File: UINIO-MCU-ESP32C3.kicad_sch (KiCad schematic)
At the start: 40 parts, among them J1 Conn_01x15_Male, J2 外接串行下载接口, J3 Conn_01x15_Male, SW1 复位按键, SW2 下载按键, U1 ME6211C33M5G-N, U2 W25Q128JVSSIQ, U3 ESP32-C3, U4 CH343P, Y1 40MHz

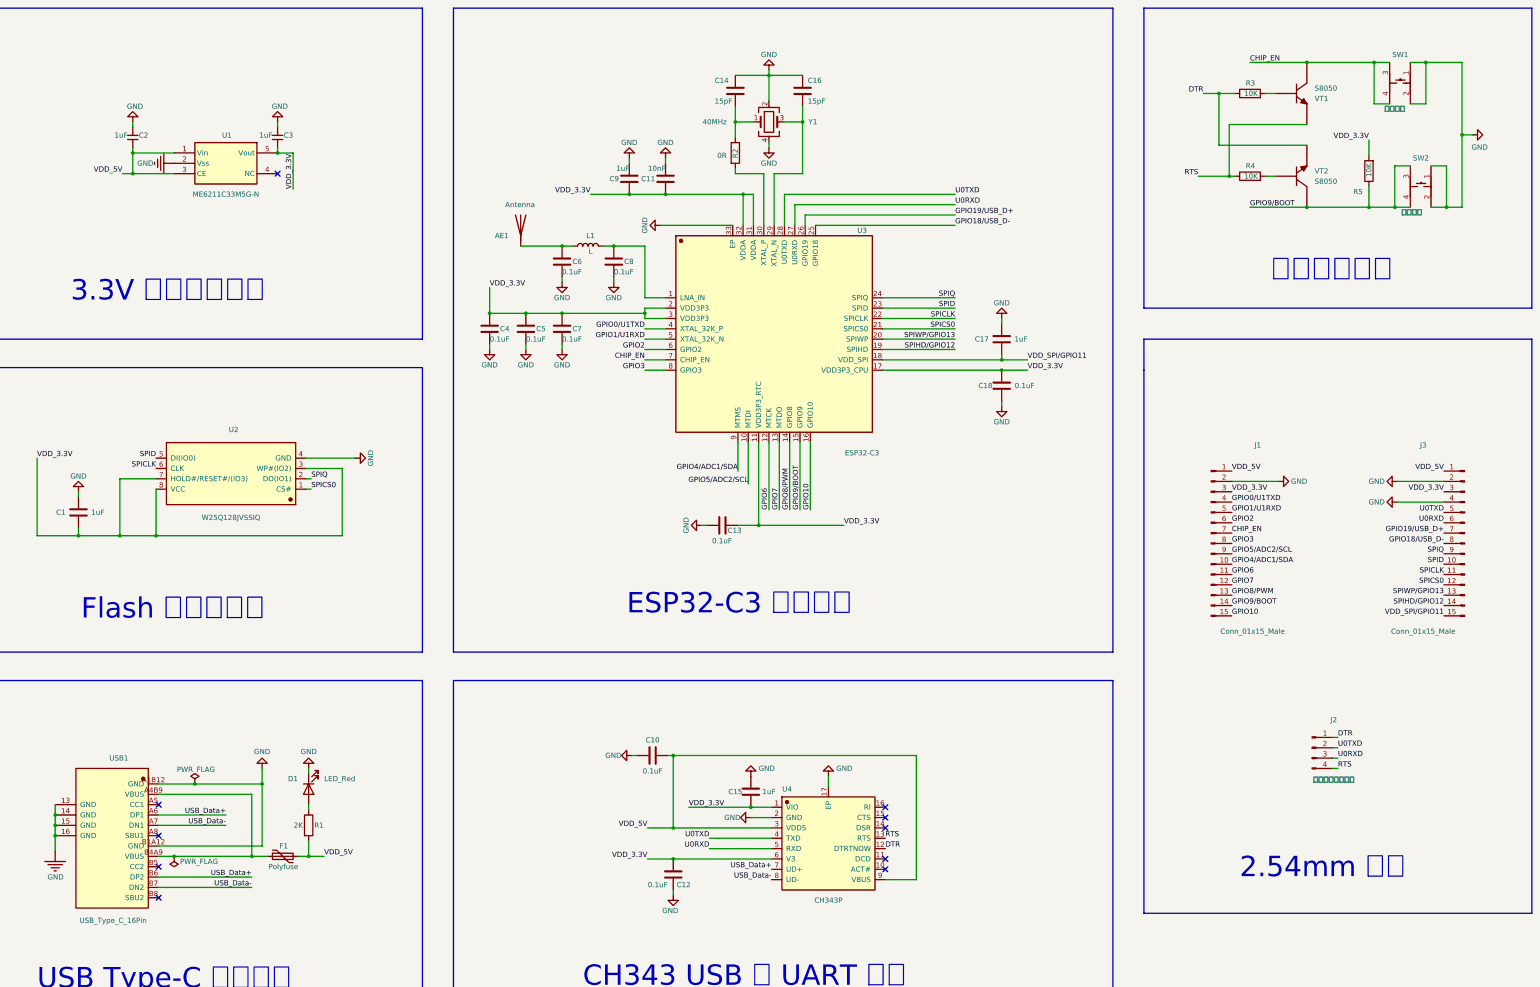
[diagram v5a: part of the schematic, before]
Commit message: The schematic diagram is drawn.
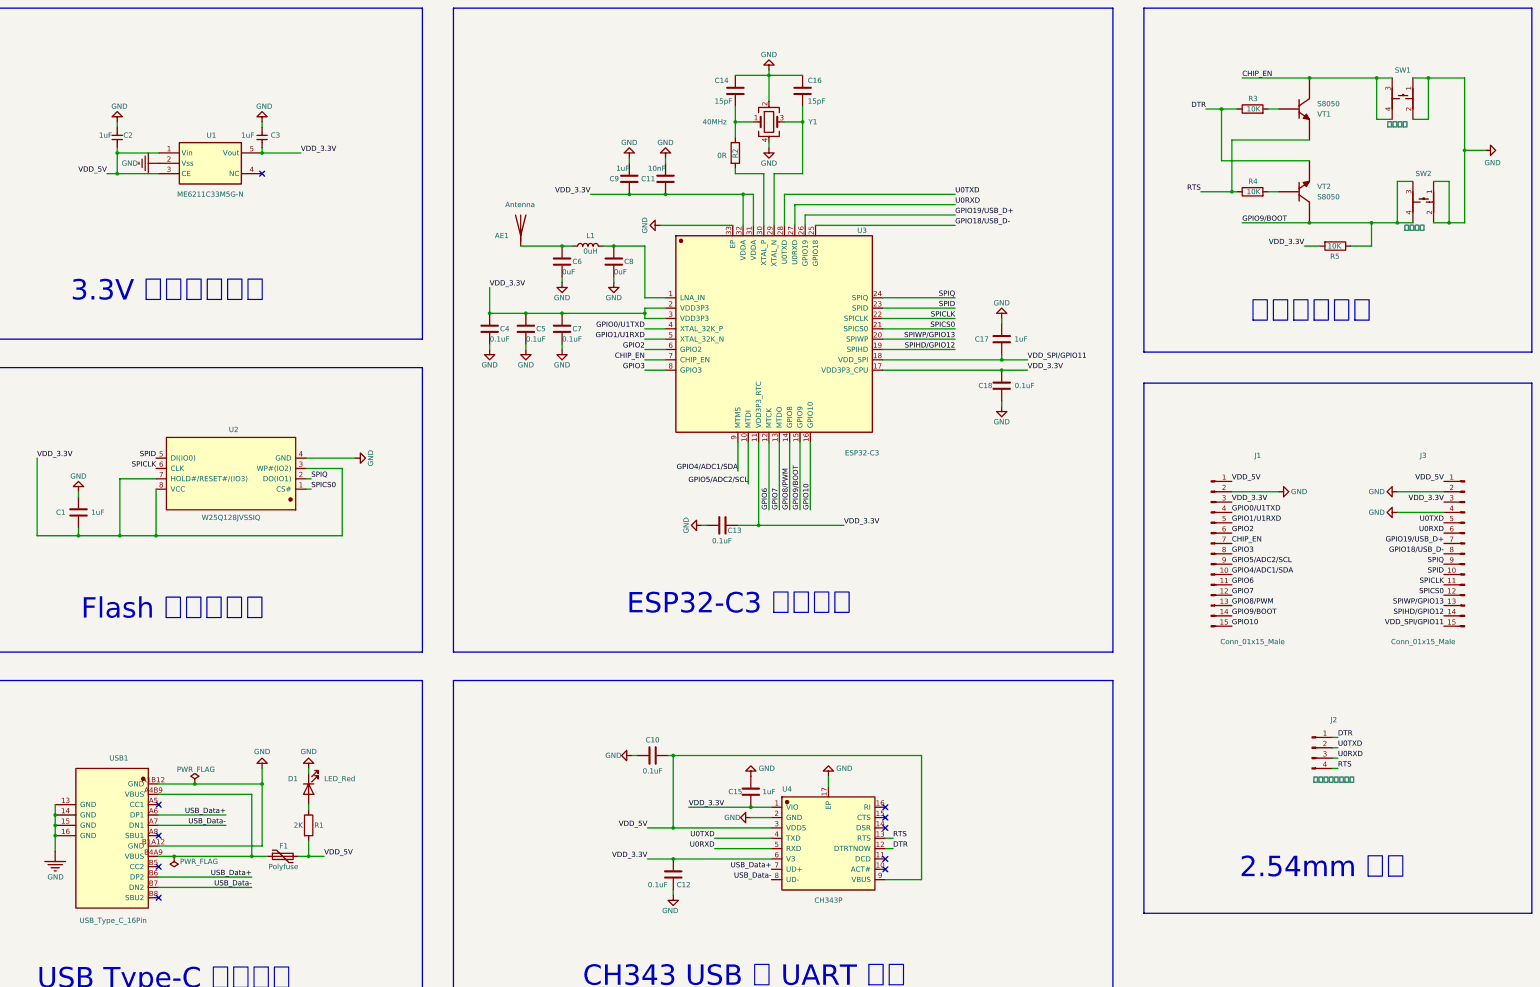
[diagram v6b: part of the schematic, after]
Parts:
- AE1: footprint (none) -> RF_Antenna:Texas_SWRA117D_2.4GHz_Left
- C1, C11, C13, C14, C16, C17, C18, C4, C5, C7, C9: footprint (none) -> Capacitor_SMD:C_0402_1005Metric
- C10, C12, C15: footprint Capacitor_SMD:C_0603_1608Metric -> Capacitor_SMD:C_0402_1005Metric
- C6, C8: value 0.1uF -> 0uF; footprint (none) -> Capacitor_SMD:C_0402_1005Metric
- J1, J3: footprint (none) -> Connector_PinHeader_2.54mm:PinHeader_1x15_P2.54mm_Vertical
- J2: footprint (none) -> Connector_PinHeader_2.54mm:PinHeader_1x04_P2.54mm_Vertical
- L1: value L -> 0uH; footprint (none) -> Inductor_SMD:L_0402_1005Metric
- R1: footprint Resistor_SMD:R_0603_1608Metric -> Resistor_SMD:R_0402_1005Metric
- R2, R3, R4, R5: footprint (none) -> Resistor_SMD:R_0402_1005Metric
- U1: footprint Uinio:SOT-23-5_L3.0-W1.7-P0.95-LS2.8-BR -> Uinio:SOT23-5
- U2: footprint kicad_lceda:SOIC-8_L5.3-W5.3-P1.27-LS8.0-BL -> Uinio:SOIC-8_L5.3-W5.3-P1.27-LS8.0-BL
- U3: footprint kicad_lceda:QFN-32_L5.0-W5.0-P0.50-TL-EP3.7 -> Uinio:QFN-32_L5.0-W5.0-P0.50-TL-EP3.7
- U4: footprint kicad_lceda:TQFN-16_L3.0-W3.0-P0.50-BL-EP1.7 -> Uinio:TQFN-16_L3.0-W3.0-P0.50-BL-EP1.7
- Y1: footprint (none) -> Crystal:Crystal_SMD_3225-4Pin_3.2x2.5mm
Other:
- moved on the sheet: C2, C3, J1, J3, R3, R4, R5, SW1, SW2, U1, VT1, VT2

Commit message: update
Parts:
- removed C2, C3: 1uF, Capacitor_SMD:C_0402_1005Metric, symbol Uinio:CAP_0402
- added C2, C3: 1uF, Capacitor_SMD:C_0402_1005Metric, symbol Device:C
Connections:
- net GND: now also C2.1, C3.1
- net VDD_3.3V: now also C3.2
- net VDD_5V: now also C2.2
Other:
- moved on the sheet: C13
